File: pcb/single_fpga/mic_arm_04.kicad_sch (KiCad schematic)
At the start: 18 parts, among them U103 CDCLVC1108PW, U33 IM72D128V01XTMA1, U34 IM72D128V01XTMA1, U35 IM72D128V01XTMA1, U36 IM72D128V01XTMA1, U37 IM72D128V01XTMA1, U38 IM72D128V01XTMA1, U39 IM72D128V01XTMA1, U40 IM72D128V01XTMA1

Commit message: Fixed symbol library references.
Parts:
- U103: footprint PW0016A_N -> CDCLVC1108:PW0016A_N
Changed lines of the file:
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@@
 			)
 		)
-		(property "Footprint" "PW0016A_N"
+		(property "Footprint" "CDCLVC1108:PW0016A_N"
 			(at 229.87 95.25 0)
 			(hide yes)

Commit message: Fixed footprints. Added missing mic. Relinked placed footprints.
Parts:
- U33, U34, U35, U36, U37, U38, U39, U40: footprint (none) -> IM72D128:IFX-PG-LLGA-5-4
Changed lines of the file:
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@@
 			)
 		)
-		(property "Footprint" ""
+		(property "Footprint" "IM72D128:IFX-PG-LLGA-5-4"
 			(at 59.69 160.02 0)
 			(hide yes)
@@
 			)
 		)
-		(property "Footprint" ""
+		(property "Footprint" "IM72D128:IFX-PG-LLGA-5-4"
 			(at 135.89 160.02 0)
 			(hide yes)
@@
 			)
 		)
-		(property "Footprint" ""
+		(property "Footprint" "IM72D128:IFX-PG-LLGA-5-4"
 			(at 59.69 83.82 0)
 			(hide yes)
@@
 			)
 		)
-		(property "Footprint" ""
+		(property "Footprint" "IM72D128:IFX-PG-LLGA-5-4"
 			(at 59.69 120.65 0)
 			(hide yes)
@@
 			)
 		)
-		(property "Footprint" ""
+		(property "Footprint" "IM72D128:IFX-PG-LLGA-5-4"
 			(at 59.69 44.45 0)
 			(hide yes)
@@
 			)
 		)
-		(property "Footprint" ""
+		(property "Footprint" "IM72D128:IFX-PG-LLGA-5-4"
 			(at 135.89 83.82 0)
 			(hide yes)
@@
 			)
 		)
-		(property "Footprint" ""
+		(property "Footprint" "IM72D128:IFX-PG-LLGA-5-4"
 			(at 135.89 44.45 0)
 			(hide yes)
@@
 			)
 		)
-		(property "Footprint" ""
+		(property "Footprint" "IM72D128:IFX-PG-LLGA-5-4"
 			(at 135.89 120.65 0)
 			(hide yes)

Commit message: Updated all refdes's.
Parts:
- removed C50, C51, C52, C53, C54, C55, C56, C57: 100nF, Capacitor_SMD:C_0603_1608Metric, symbol Device:C
- removed R9: 10k, PCM_SparkFun-Resistor:R_0603_1608Metric, symbol PCM_SparkFun-Resistor:10k_0603
- removed U103: CDCLVC1108PW, CDCLVC1108:PW0016A_N, symbol CDCLVC1108:CDCLVC1108PW
- removed U33, U34, U35, U36: IM72D128V01XTMA1, IM72D128:IFX-PG-LLGA-5-4, symbol multi_fpga:IM72D128
- added C33, C34, C35, C36, C37, C38, C39, C40: 100nF, Capacitor_SMD:C_0603_1608Metric, symbol Device:C
- added R5: 10k, PCM_SparkFun-Resistor:R_0603_1608Metric, symbol PCM_SparkFun-Resistor:10k_0603
- added U41, U42, U43, U44: IM72D128V01XTMA1, IM72D128:IFX-PG-LLGA-5-4, symbol multi_fpga:IM72D128
- added U45: CDCLVC1108PW, CDCLVC1108:PW0016A_N, symbol CDCLVC1108:CDCLVC1108PW
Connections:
- net ARM_04_CLK: now also U45.1 (CLKIN)
- net CLK_3V3: now also R5.2, U45.10 (VDD), U45.14 (VDD), U45.5 (VDD)
- net DATA_16: now also U37.1 (DATA), U38.1 (DATA)
- net DATA_17: now also U39.1 (DATA), U40.1 (DATA)
- net DATA_18: now also U41.1 (DATA), U42.1 (DATA); no longer U37.1 (DATA), U38.1 (DATA)
- net DATA_19: now also U43.1 (DATA), U44.1 (DATA); no longer U39.1 (DATA), U40.1 (DATA)
- net GND: now also C33.2, C34.2, C35.2, C36.2, C37.2, C38.2, C39.2, C40.2, U41.4 (SEL), U41.5 (GND), U42.5 (GND), U43.4 (SEL), U43.5 (GND), U44.5 (GND), U45.12 (GND), U45.4 (GND), U45.7 (GND)
- net MIC_3V3: now also C33.1, C34.1, C35.1, C36.1, C37.1, C38.1, C39.1, C40.1, U41.2 (VDD), U42.2 (VDD), U42.4 (SEL), U43.2 (VDD), U44.2 (VDD), U44.4 (SEL)
- net MIC_CLK_32: now also U37.3 (CLK), U45.3 (Y0)
- net MIC_CLK_33: now also U38.3 (CLK), U45.16 (Y1)
- net MIC_CLK_34: now also U39.3 (CLK), U45.13 (Y2)
- net MIC_CLK_35: now also U40.3 (CLK), U45.15 (Y3)
- net MIC_CLK_36: now also U41.3 (CLK), U45.6 (Y4); no longer U37.3 (CLK)
- net MIC_CLK_37: now also U42.3 (CLK), U45.11 (Y5); no longer U38.3 (CLK)
- net MIC_CLK_38: now also U43.3 (CLK), U45.8 (Y6); no longer U39.3 (CLK)
- net MIC_CLK_39: now also U44.3 (CLK), U45.9 (Y7); no longer U40.3 (CLK)
- new net: R5.1, U45.2 (1G)

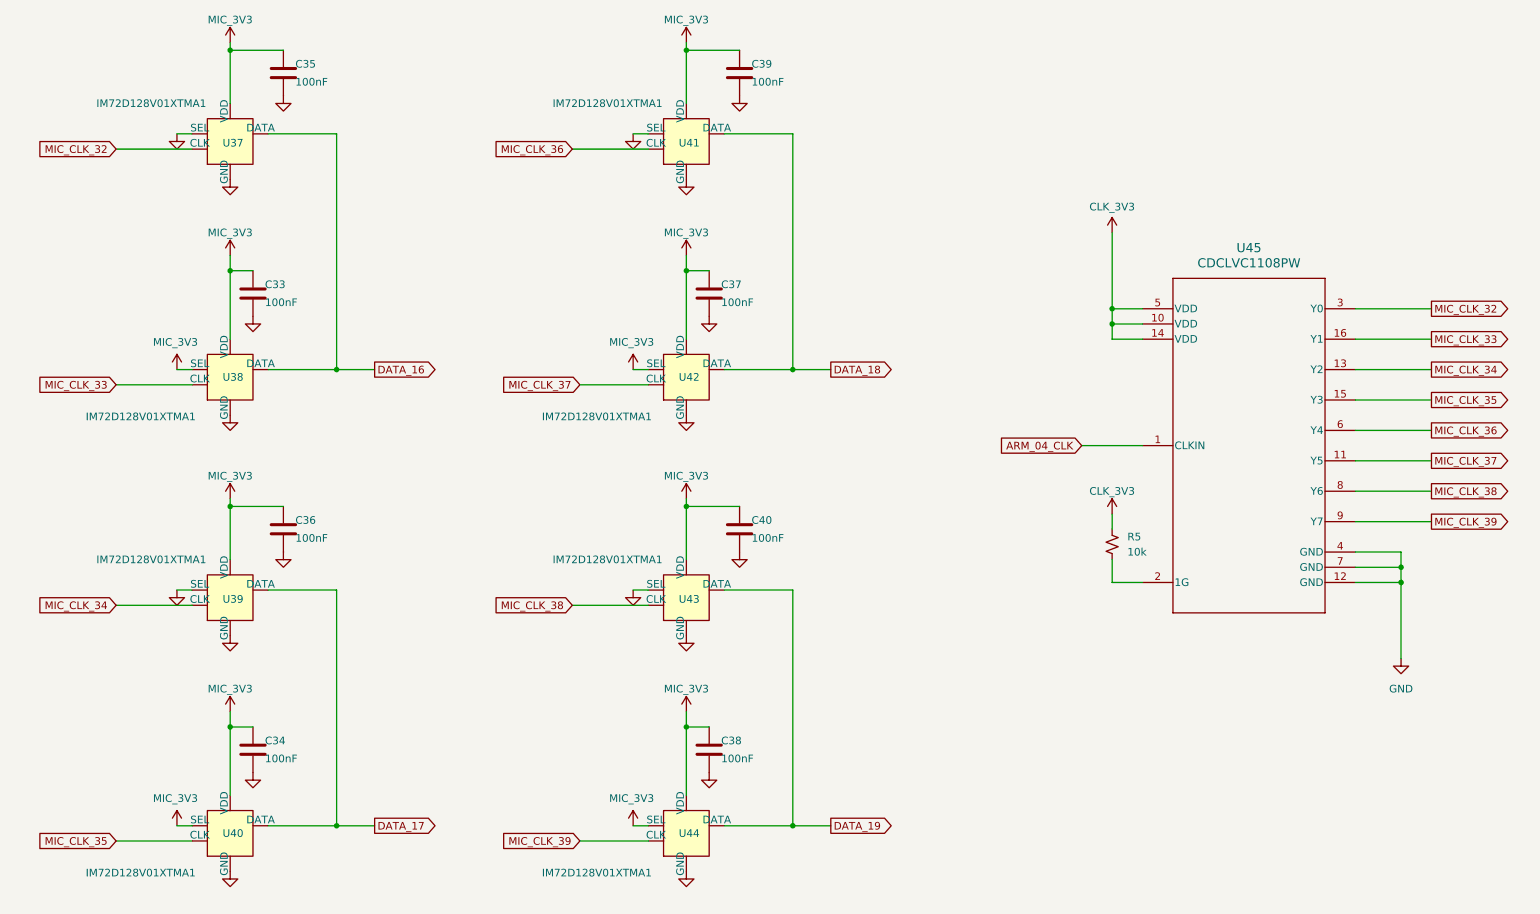
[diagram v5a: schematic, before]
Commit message: Changed mic symbol to improve readability.
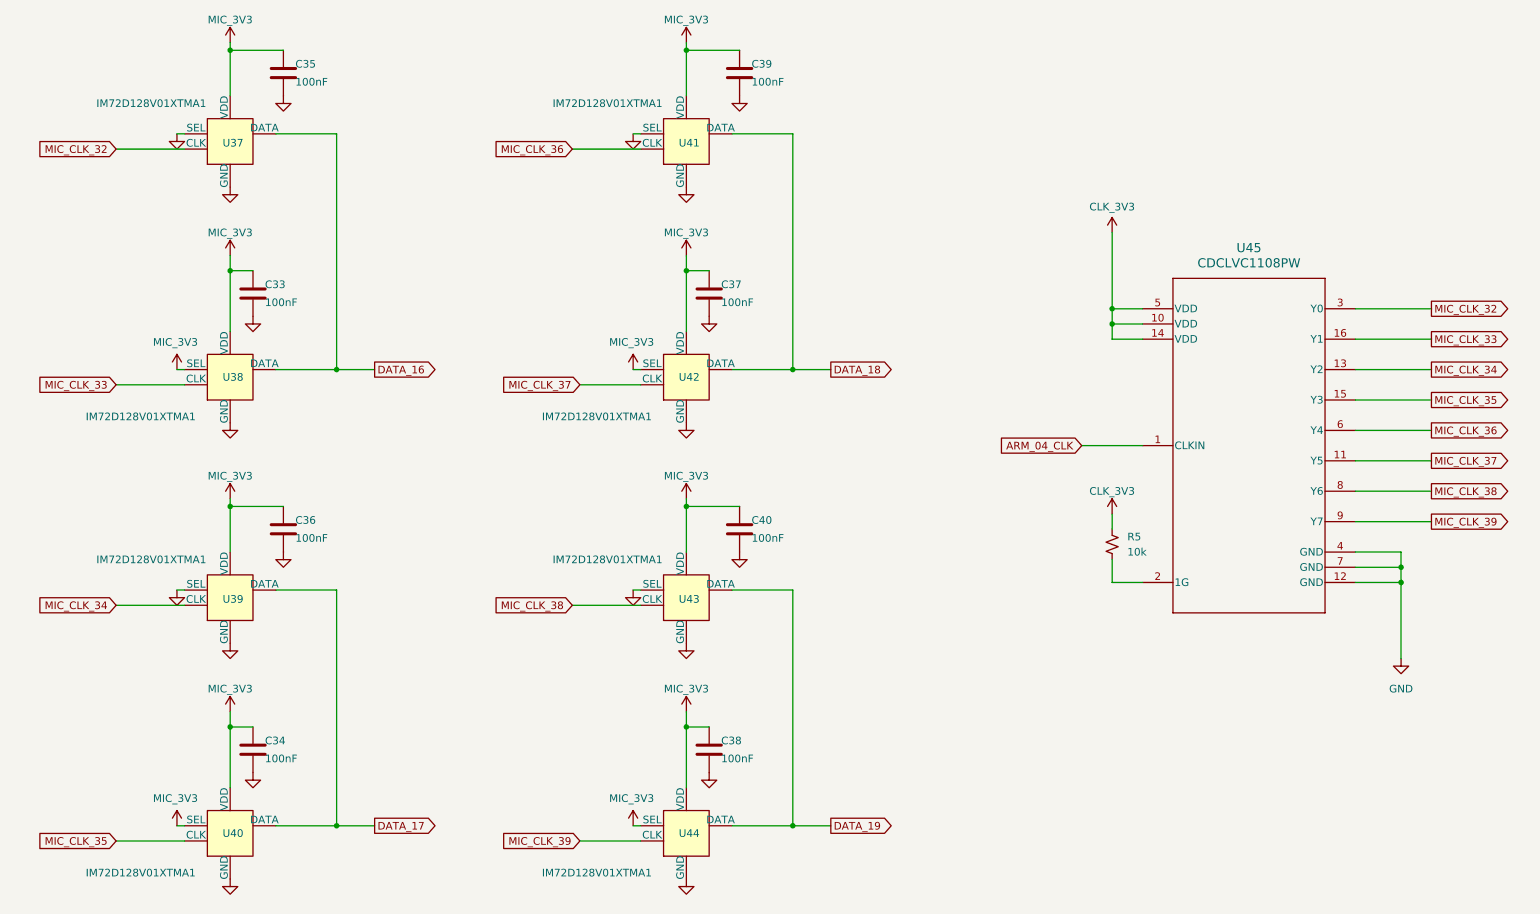
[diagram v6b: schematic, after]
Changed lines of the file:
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@@
 	(wire
 		(pts
-			(xy 116.84 45.72) (xy 129.54 45.72)
+			(xy 116.84 45.72) (xy 128.27 45.72)
 		)
 		(stroke
@@
 	(wire
 		(pts
-			(xy 135.89 142.24) (xy 135.89 153.67)
+			(xy 135.89 142.24) (xy 135.89 152.4)
 		)
 		(stroke
@@
 	(wire
 		(pts
-			(xy 135.89 105.41) (xy 135.89 114.3)
+			(xy 135.89 105.41) (xy 135.89 113.03)
 		)
 		(stroke
@@
 	(wire
 		(pts
-			(xy 118.11 85.09) (xy 129.54 85.09)
+			(xy 118.11 85.09) (xy 128.27 85.09)
 		)
 		(stroke
@@
 	(wire
 		(pts
-			(xy 59.69 142.24) (xy 59.69 153.67)
+			(xy 59.69 142.24) (xy 59.69 152.4)
 		)
 		(stroke
@@
 	(wire
 		(pts
-			(xy 66.04 82.55) (xy 77.47 82.55)
+			(xy 67.31 82.55) (xy 77.47 82.55)
 		)
 		(stroke
@@
 	(wire
 		(pts
-			(xy 127 119.38) (xy 129.54 119.38)
+			(xy 127 119.38) (xy 128.27 119.38)
 		)
 		(stroke
@@
 	(wire
 		(pts
-			(xy 118.11 161.29) (xy 129.54 161.29)
+			(xy 118.11 161.29) (xy 128.27 161.29)
 		)
 		(stroke
@@
 	(wire
 		(pts
-			(xy 59.69 29.21) (xy 59.69 38.1)
+			(xy 59.69 29.21) (xy 59.69 36.83)
 		)
 		(stroke
@@
 	(wire
 		(pts
-			(xy 40.64 85.09) (xy 53.34 85.09)
+			(xy 40.64 85.09) (xy 52.07 85.09)
 		)
 		(stroke
@@
 	(wire
 		(pts
-			(xy 127 43.18) (xy 129.54 43.18)
+			(xy 127 43.18) (xy 128.27 43.18)
 		)
 		(stroke
@@
 	(wire
 		(pts
-			(xy 127 82.55) (xy 129.54 82.55)
+			(xy 127 82.55) (xy 128.27 82.55)
 		)
 		(stroke
@@
 	(wire
 		(pts
-			(xy 135.89 29.21) (xy 135.89 38.1)
+			(xy 135.89 29.21) (xy 135.89 36.83)
 		)
 		(stroke
@@
 	(wire
 		(pts
-			(xy 40.64 45.72) (xy 53.34 45.72)
+			(xy 40.64 45.72) (xy 52.07 45.72)
 		)
 		(stroke
@@
 	(wire
 		(pts
-			(xy 77.47 43.18) (xy 66.04 43.18)
+			(xy 77.47 43.18) (xy 67.31 43.18)
 		)
 		(stroke
@@
 	(wire
 		(pts
-			(xy 135.89 66.04) (xy 135.89 77.47)
+			(xy 135.89 66.04) (xy 135.89 76.2)
 		)
 		(stroke
@@
 	(wire
 		(pts
-			(xy 127 158.75) (xy 129.54 158.75)
+			(xy 127 158.75) (xy 128.27 158.75)
 		)
 		(stroke
@@
 	(wire
 		(pts
-			(xy 50.8 158.75) (xy 53.34 158.75)
+			(xy 50.8 158.75) (xy 52.07 158.75)
 		)
 		(stroke
@@
 	(wire
 		(pts
-			(xy 50.8 82.55) (xy 53.34 82.55)
+			(xy 50.8 82.55) (xy 52.07 82.55)
 		)
 		(stroke
@@
 	(wire
 		(pts
-			(xy 153.67 119.38) (xy 142.24 119.38)
+			(xy 153.67 119.38) (xy 143.51 119.38)
 		)
 		(stroke
@@
 	(wire
 		(pts
-			(xy 77.47 119.38) (xy 66.04 119.38)
+			(xy 77.47 119.38) (xy 67.31 119.38)
 		)
 		(stroke
@@
 	(wire
 		(pts
-			(xy 142.24 82.55) (xy 153.67 82.55)
+			(xy 143.51 82.55) (xy 153.67 82.55)
 		)
 		(stroke
@@
 	(wire
 		(pts
-			(xy 153.67 43.18) (xy 142.24 43.18)
+			(xy 153.67 43.18) (xy 143.51 43.18)
 		)
 		(stroke
@@
 	(wire
 		(pts
-			(xy 40.64 121.92) (xy 53.34 121.92)
+			(xy 40.64 121.92) (xy 52.07 121.92)
 		)
 		(stroke
@@
 	(wire
 		(pts
-			(xy 40.64 161.29) (xy 53.34 161.29)
+			(xy 40.64 161.29) (xy 52.07 161.29)
 		)
 		(stroke
@@
 	(wire
 		(pts
-			(xy 50.8 43.18) (xy 53.34 43.18)
+			(xy 50.8 43.18) (xy 52.07 43.18)
 		)
 		(stroke
@@
 	(wire
 		(pts
-			(xy 59.69 105.41) (xy 59.69 114.3)
+			(xy 59.69 105.41) (xy 59.69 113.03)
 		)
 		(stroke
@@
 	(wire
 		(pts
-			(xy 66.04 158.75) (xy 77.47 158.75)
+			(xy 67.31 158.75) (xy 77.47 158.75)
 		)
 		(stroke
@@
 	(wire
 		(pts
-			(xy 142.24 158.75) (xy 153.67 158.75)
+			(xy 143.51 158.75) (xy 153.67 158.75)
 		)
 		(stroke
@@
 	(wire
 		(pts
-			(xy 50.8 119.38) (xy 53.34 119.38)
+			(xy 50.8 119.38) (xy 52.07 119.38)
 		)
 		(stroke
@@
 	(wire
 		(pts
-			(xy 116.84 121.92) (xy 129.54 121.92)
+			(xy 116.84 121.92) (xy 128.27 121.92)
 		)
 		(stroke
@@
 	(wire
 		(pts
-			(xy 59.69 66.04) (xy 59.69 77.47)
+			(xy 59.69 66.04) (xy 59.69 76.2)
 		)
 		(stroke
@@
 	(symbol
 		(lib_id "power:GND")
-		(at 135.89 166.37 0)
+		(at 135.89 167.64 0)
 		(unit 1)
 		(body_style 1)
@@
 	(symbol
 		(lib_id "power:GND")
-		(at 59.69 166.37 0)
+		(at 59.69 167.64 0)
 		(unit 1)
 		(body_style 1)
@@
 	(symbol
 		(lib_id "power:GND")
-		(at 59.69 50.8 0)
+		(at 59.69 52.07 0)
 		(unit 1)
 		(body_style 1)
@@
 	(symbol
 		(lib_id "power:GND")
-		(at 59.69 90.17 0)
+		(at 59.69 91.44 0)
 		(unit 1)
 		(body_style 1)
@@
 	(symbol
 		(lib_id "power:GND")
-		(at 135.89 127 0)
+		(at 135.89 128.27 0)
 		(unit 1)
 		(body_style 1)
@@
 	(symbol
 		(lib_id "power:GND")
-		(at 135.89 50.8 0)
+		(at 135.89 52.07 0)
 		(unit 1)
 		(body_style 1)
@@
 	(symbol
 		(lib_id "power:GND")
-		(at 59.69 127 0)
+		(at 59.69 128.27 0)
 		(unit 1)
 		(body_style 1)
@@
 	(symbol
 		(lib_id "power:GND")
-		(at 135.89 90.17 0)
+		(at 135.89 91.44 0)
 		(unit 1)
 		(body_style 1)

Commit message: Used new mic symbol and cleaned up.
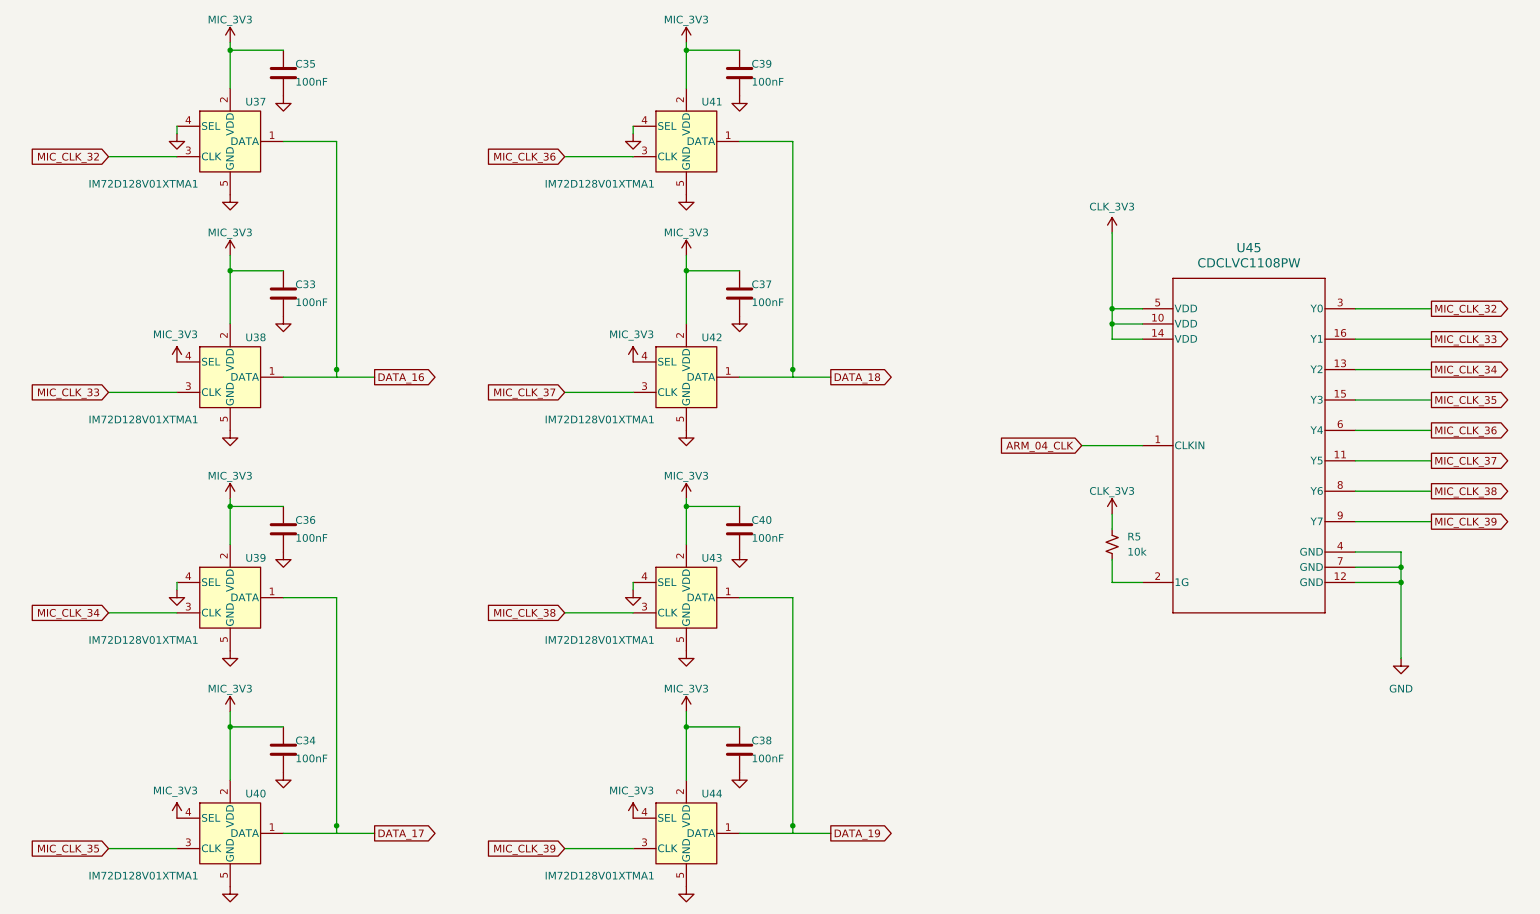
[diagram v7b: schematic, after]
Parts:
- U37, U38, U39, U40, U41, U42, U43, U44: footprint IM72D128:IFX-PG-LLGA-5-4 -> (none)
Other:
- moved on the sheet: C33, C34, C37, C38
